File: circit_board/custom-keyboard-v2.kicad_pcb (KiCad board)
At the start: 2 copper layers, 266 x 99.8 mm, 141 parts, among them J1 i2c_display, J2 Adafruit-AP3602A-PCB, SW1 SW_Push, SW10 SW_Push, SW11 SW_Push, SW12 SW_Push, SW13 SW_Push, SW14 SW_Push, SW15 SW_Push, SW16 SW_Push, SW17 SW_Push, SW18 SW_Push, SW19 SW_Push, SW2 SW_Push, SW20 SW_Push, SW21 SW_Push, SW22 SW_Push, SW23 SW_Push, SW24 SW_Push, SW25 SW_Push, SW26 SW_Push, SW27 SW_Push, SW28 SW_Push, SW29 SW_Push, SW3 SW_Push, SW30 SW_Push, SW31 SW_Push, SW32 SW_Push, SW33 SW_Push, SW34 SW_Push, SW35 SW_Push, SW36 SW_Push, SW37 SW_Push, SW38 SW_Push, SW39 SW_Push, SW4 SW_Push, SW40 SW_Push, SW41 SW_Push, SW42 SW_Push, SW43 SW_Push, SW44 SW_Push, SW45 SW_Push, SW46 SW_Push, SW5 SW_Push, SW6 SW_Push, SW7 SW_Push, SW8 SW_Push, SW9 SW_Push

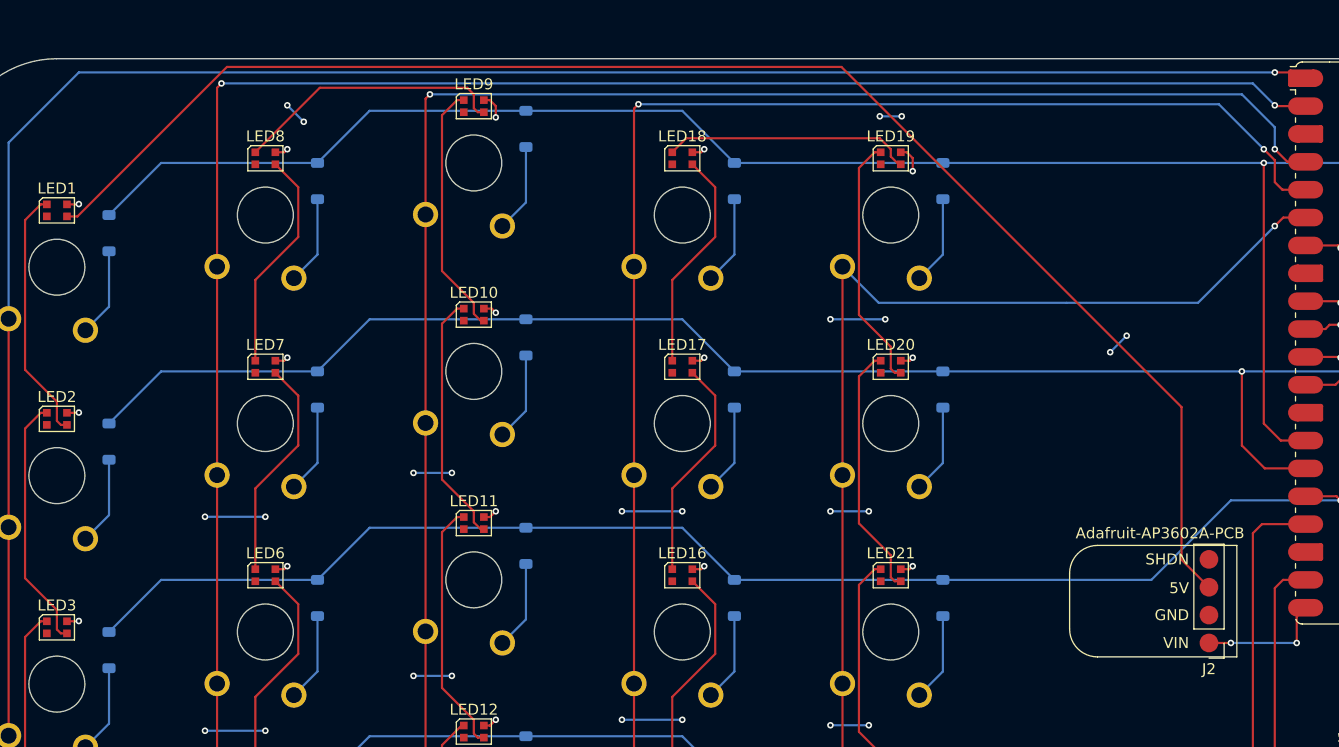
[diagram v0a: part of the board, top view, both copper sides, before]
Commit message: Removed 3.3V to 5V converter from the LED input
This turned out to be unnecessary after getting the circit board printed
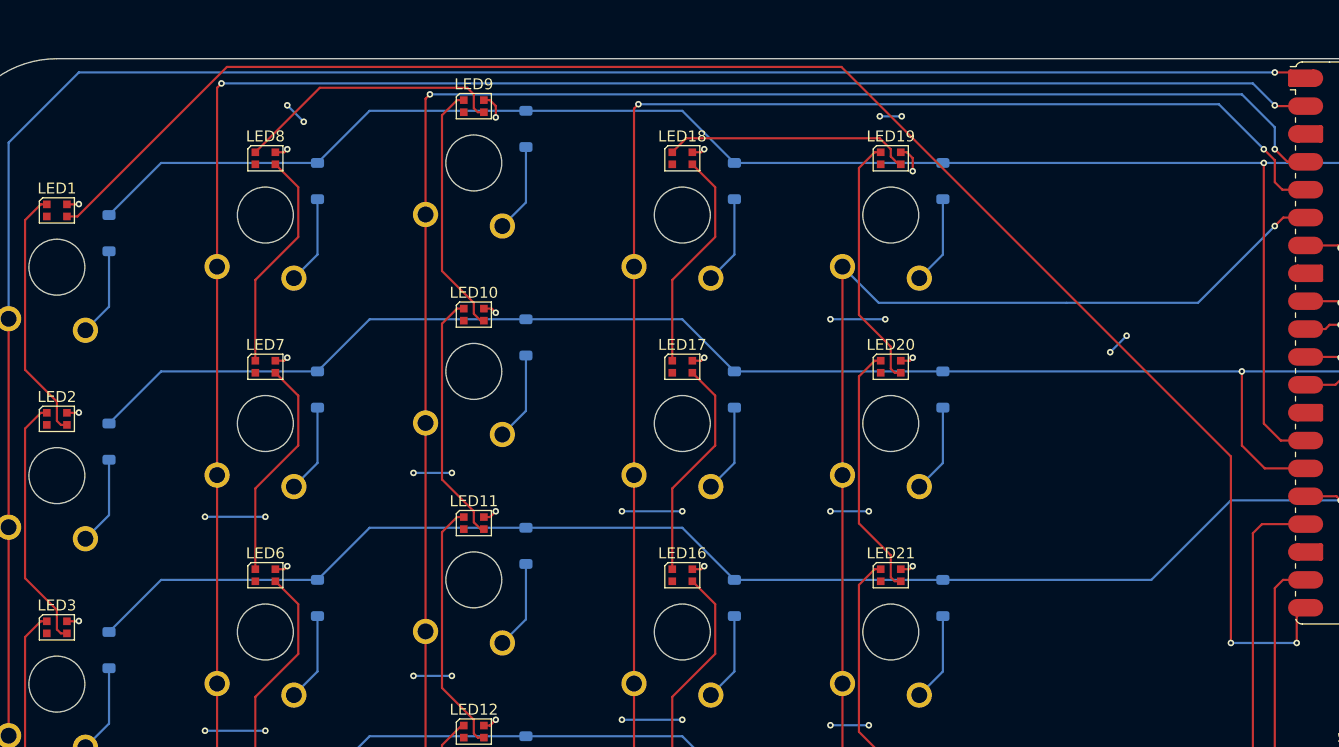
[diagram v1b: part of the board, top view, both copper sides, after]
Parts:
- removed J2: Adafruit-AP3602A-PCB, Connector_PinHeader_2.54mm:PinHeader_1x04_P2.54mm_Vertical
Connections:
- A1 pad 20: Net-(A1-GPIO15) -> led-data
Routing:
- net led-data: track 137.5 -> 153.0 mm, vias 0 -> 2
- net Net-(A1-GPIO15): track 11.5 -> 0.00 mm, vias 2 -> 0
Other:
- board text removed: "5V"
- board text removed: "SHDN"
- board text removed: "VIN"
